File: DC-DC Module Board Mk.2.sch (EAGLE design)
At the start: 151 parts, among them T1 FDN340P, T2 AP1117_LIN_REG, U3 LM1085IS-5.0

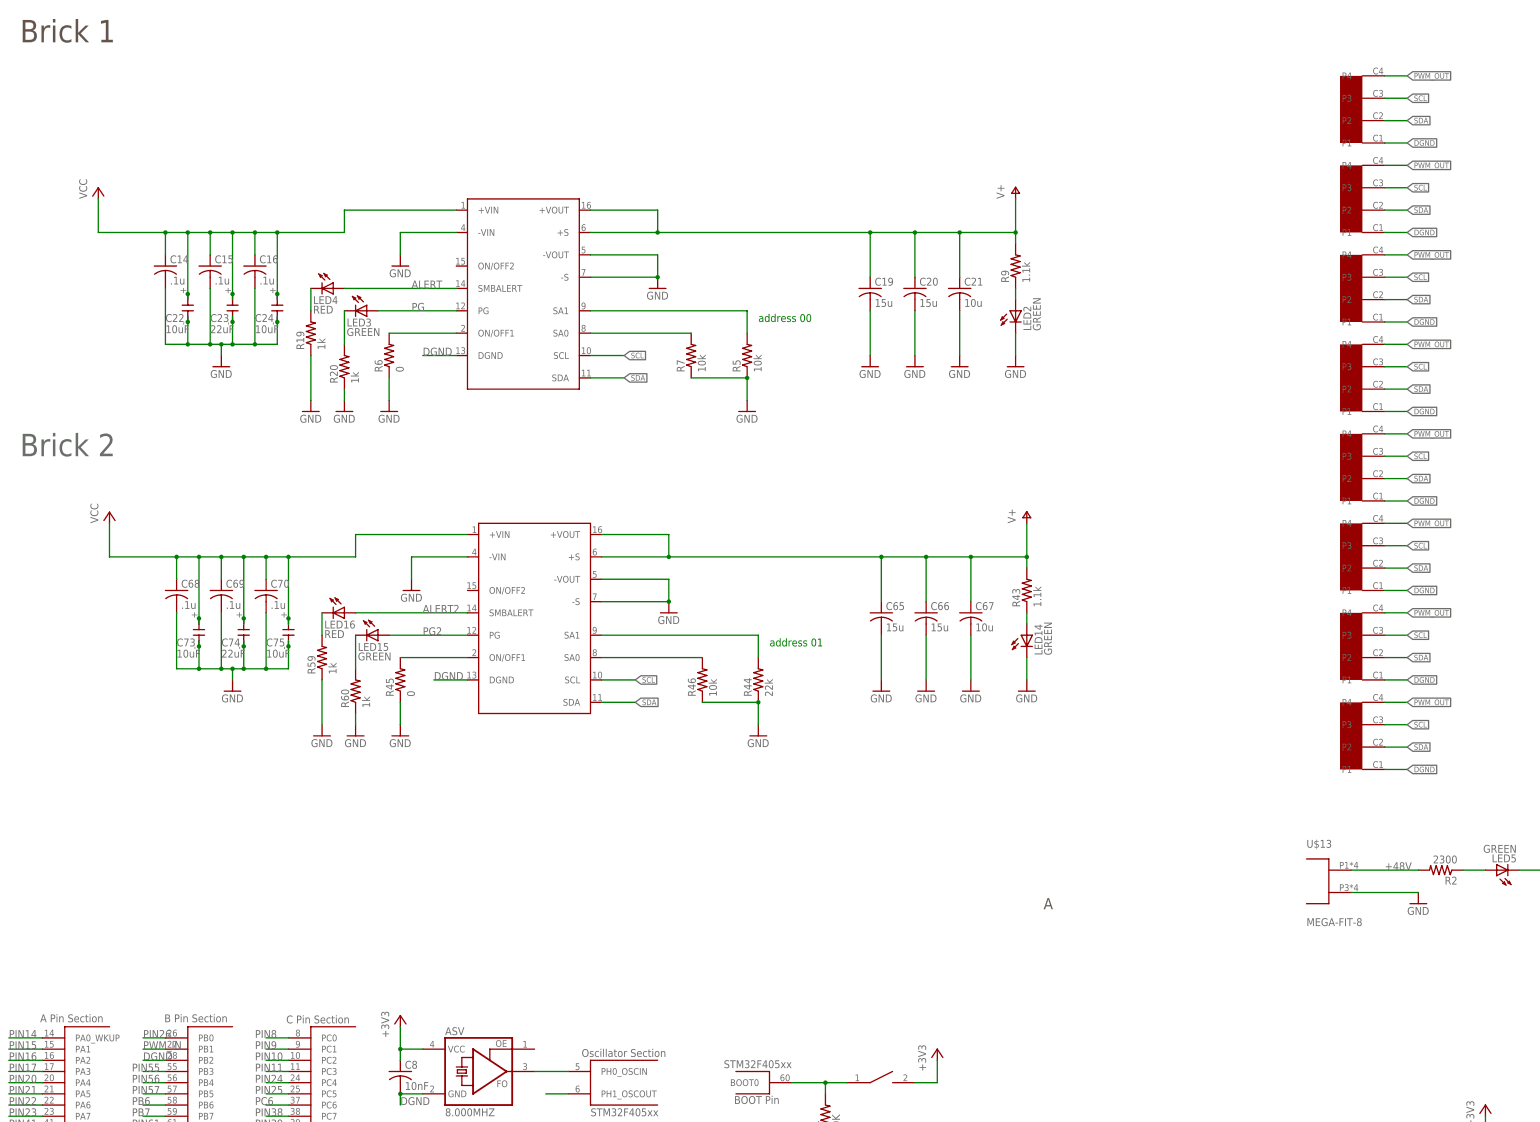
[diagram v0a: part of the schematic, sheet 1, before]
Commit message: changed pwm signal to thrusters
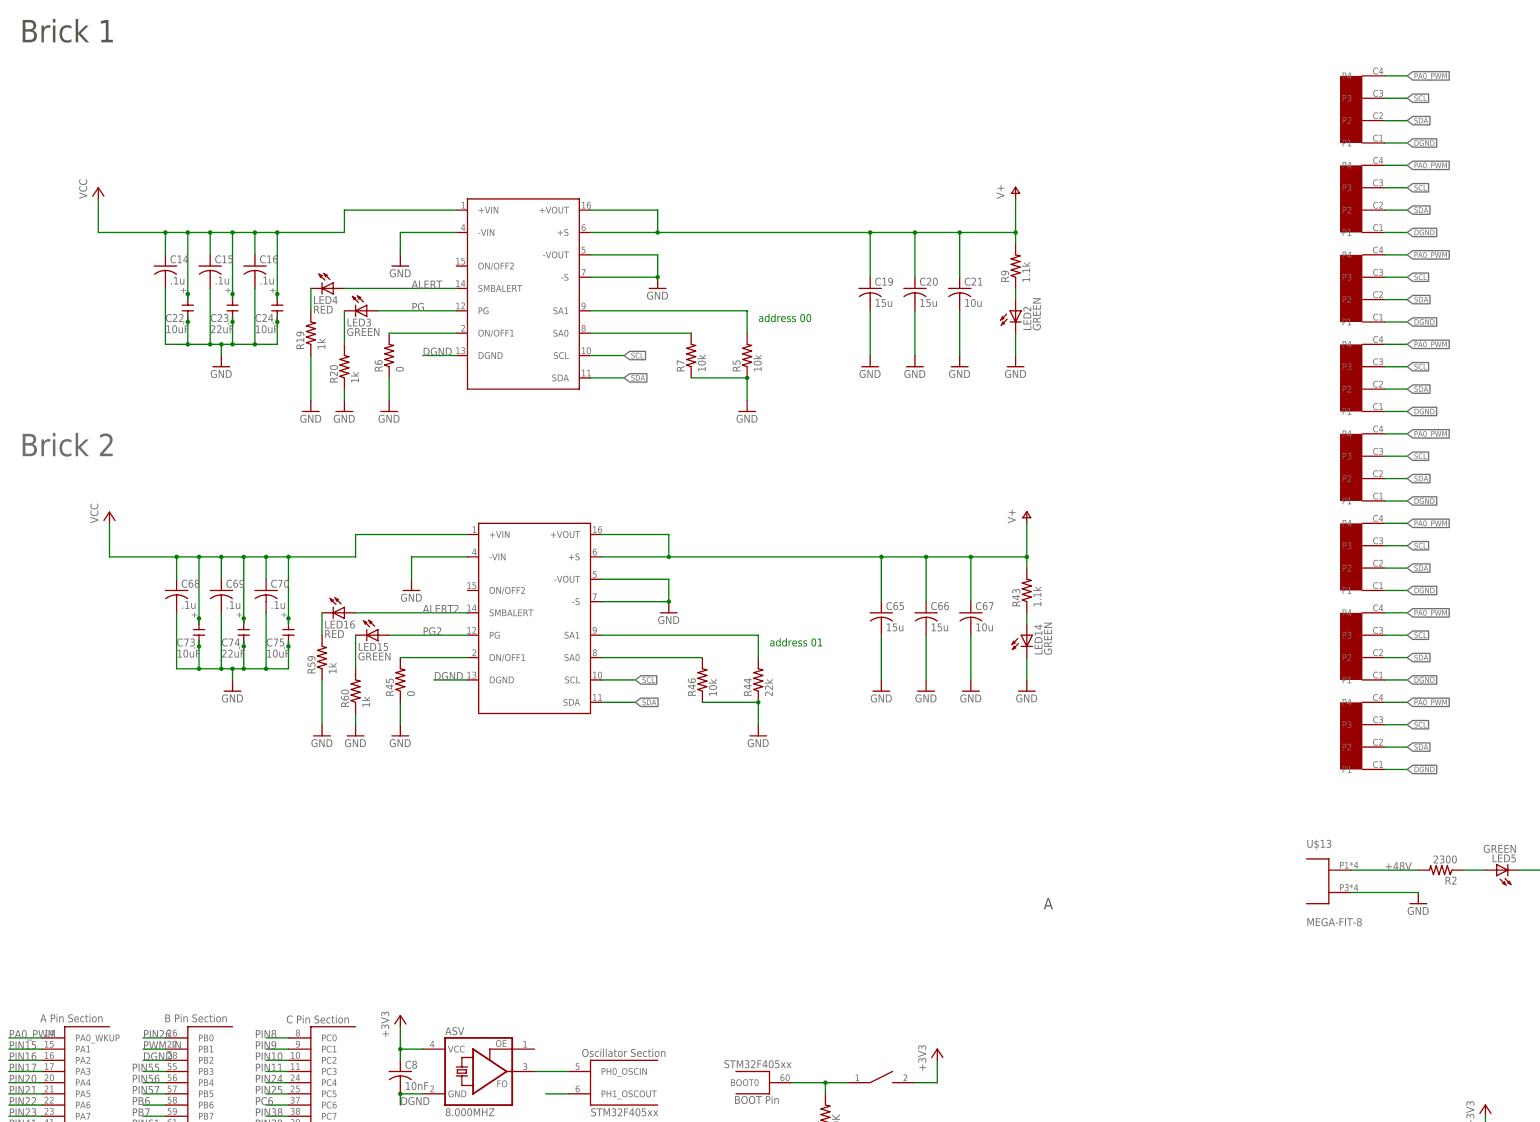
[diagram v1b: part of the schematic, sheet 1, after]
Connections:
- removed net PIN14: U$5G$1.PA0_WKUP
- new net PA0_PWM: U$15.P4, U$20.P4, U$23.P4, U$24.P4, U$25.P4, U$26.P4, U$27.P4, U$28.P4, U$5G$1.PA0_WKUP
- net PWM_OUT: no longer U$15.P4, U$20.P4, U$23.P4, U$24.P4, U$25.P4, U$26.P4, U$27.P4, U$28.P4
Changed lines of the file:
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@@
 </segment>
 </net>
-<net name="PIN14" class="0">
+<net name="PA0_PWM" class="0">
 <segment>
 <pinref part="U$5" gate="G$1" pin="PA0_WKUP"/>
 <wire x1="17.78" y1="-17.78" x2="10.16" y2="-17.78" width="0.1524" layer="91"/>
 <label x="10.16" y="-17.78" size="1.778" layer="95"/>
+</segment>
+<segment>
+<pinref part="U$20" gate="G$1" pin="P4"/>
+<wire x1="322.58" y1="180.34" x2="327.66" y2="180.34" width="0.1524" layer="91"/>
+<label x="327.66" y="180.34" size="1.27" layer="95" xref="yes"/>
+</segment>
+<segment>
+<pinref part="U$15" gate="G$1" pin="P4"/>
+<wire x1="322.58" y1="200.66" x2="327.66" y2="200.66" width="0.1524" layer="91"/>
+<label x="327.66" y="200.66" size="1.27" layer="95" xref="yes"/>
+</segment>
+<segment>
+<pinref part="U$23" gate="G$1" pin="P4"/>
+<wire x1="322.58" y1="160.02" x2="327.66" y2="160.02" width="0.1524" layer="91"/>
+<label x="327.66" y="160.02" size="1.27" layer="95" xref="yes"/>
+</segment>
+<segment>
+<pinref part="U$24" gate="G$1" pin="P4"/>
+<wire x1="322.58" y1="139.7" x2="327.66" y2="139.7" width="0.1524" layer="91"/>
+<label x="327.66" y="139.7" size="1.27" layer="95" xref="yes"/>
+</segment>
+<segment>
+<pinref part="U$25" gate="G$1" pin="P4"/>
+<wire x1="322.58" y1="119.38" x2="327.66" y2="119.38" width="0.1524" layer="91"/>
+<label x="327.66" y="119.38" size="1.27" layer="95" xref="yes"/>
+</segment>
+<segment>
+<pinref part="U$26" gate="G$1" pin="P4"/>
+<wire x1="322.58" y1="99.06" x2="327.66" y2="99.06" width="0.1524" layer="91"/>
+<label x="327.66" y="99.06" size="1.27" layer="95" xref="yes"/>
+</segment>
+<segment>
+<pinref part="U$27" gate="G$1" pin="P4"/>
+<wire x1="322.58" y1="78.74" x2="327.66" y2="78.74" width="0.1524" layer="91"/>
+<label x="327.66" y="78.74" size="1.27" layer="95" xref="yes"/>
+</segment>
+<segment>
+<pinref part="U$28" gate="G$1" pin="P4"/>
+<wire x1="322.58" y1="58.42" x2="327.66" y2="58.42" width="0.1524" layer="91"/>
+<label x="327.66" y="58.42" size="1.27" layer="95" xref="yes"/>
 </segment>
 </net>
@@
 <label x="441.96" y="167.64" size="1.27" layer="95" xref="yes"/>
 </segment>
-<segment>
-<pinref part="U$28" gate="G$1" pin="P4"/>
-<wire x1="322.58" y1="58.42" x2="327.66" y2="58.42" width="0.1524" layer="91"/>
-<label x="327.66" y="58.42" size="1.27" layer="95" xref="yes"/>
-</segment>
-<segment>
-<pinref part="U$15" gate="G$1" pin="P4"/>
-<wire x1="322.58" y1="200.66" x2="327.66" y2="200.66" width="0.1524" layer="91"/>
-<label x="327.66" y="200.66" size="1.27" layer="95" xref="yes"/>
-</segment>
-<segment>
-<pinref part="U$20" gate="G$1" pin="P4"/>
-<wire x1="322.58" y1="180.34" x2="327.66" y2="180.34" width="0.1524" layer="91"/>
-<label x="327.66" y="180.34" size="1.27" layer="95" xref="yes"/>
-</segment>
-<segment>
-<pinref part="U$23" gate="G$1" pin="P4"/>
-<wire x1="322.58" y1="160.02" x2="327.66" y2="160.02" width="0.1524" layer="91"/>
-<label x="327.66" y="160.02" size="1.27" layer="95" xref="yes"/>
-</segment>
-<segment>
-<pinref part="U$24" gate="G$1" pin="P4"/>
-<wire x1="322.58" y1="139.7" x2="327.66" y2="139.7" width="0.1524" layer="91"/>
-<label x="327.66" y="139.7" size="1.27" layer="95" xref="yes"/>
-</segment>
-<segment>
-<pinref part="U$25" gate="G$1" pin="P4"/>
-<wire x1="322.58" y1="119.38" x2="327.66" y2="119.38" width="0.1524" layer="91"/>
-<label x="327.66" y="119.38" size="1.27" layer="95" xref="yes"/>
-</segment>
-<segment>
-<pinref part="U$26" gate="G$1" pin="P4"/>
-<wire x1="322.58" y1="99.06" x2="327.66" y2="99.06" width="0.1524" layer="91"/>
-<label x="327.66" y="99.06" size="1.27" layer="95" xref="yes"/>
-</segment>
-<segment>
-<pinref part="U$27" gate="G$1" pin="P4"/>
-<wire x1="322.58" y1="78.74" x2="327.66" y2="78.74" width="0.1524" layer="91"/>
-<label x="327.66" y="78.74" size="1.27" layer="95" xref="yes"/>
-</segment>
-</net>
+</net>

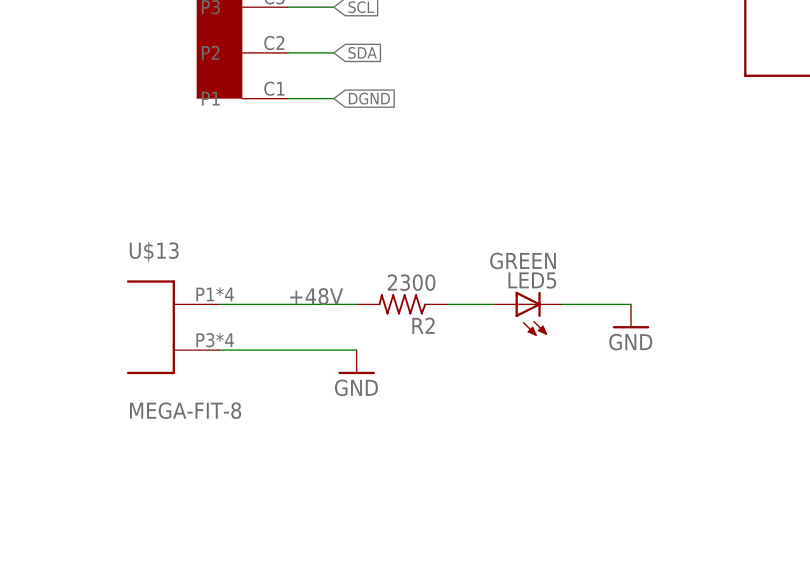
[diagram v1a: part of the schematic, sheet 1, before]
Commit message: sizing and aesthetic changes
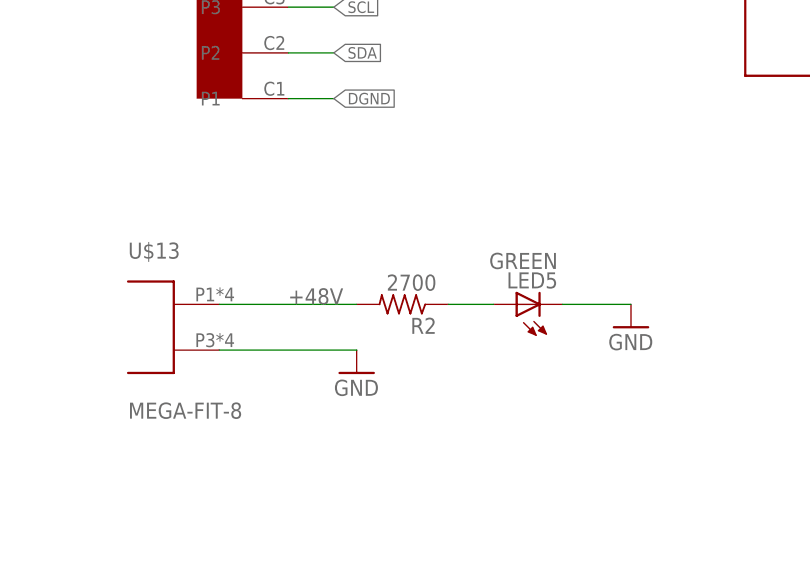
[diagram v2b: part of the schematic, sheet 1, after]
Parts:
- R2: value 2300 -> 2700
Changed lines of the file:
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@@
 <attribute name="PARTNO" value="160-1446-1-ND"/>
 </part>
-<part name="R2" library="resistor" deviceset="R-US_" device="R2512" value="2300">
+<part name="R2" library="resistor" deviceset="R-US_" device="R2512" value="2700">
 <attribute name="BOM" value="INCLUDE"/>
 <attribute name="PARTNO" value="RHC2512FT2K20CT-ND"/>

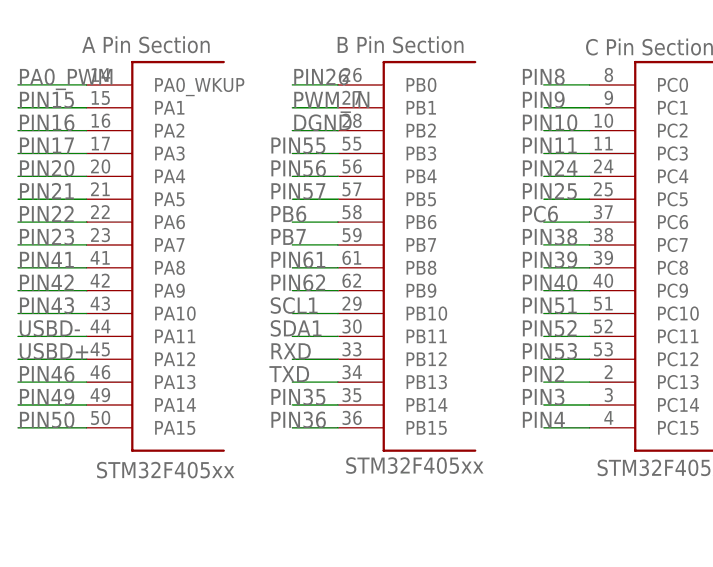
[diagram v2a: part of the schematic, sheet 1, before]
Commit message: Changed pins for i2c
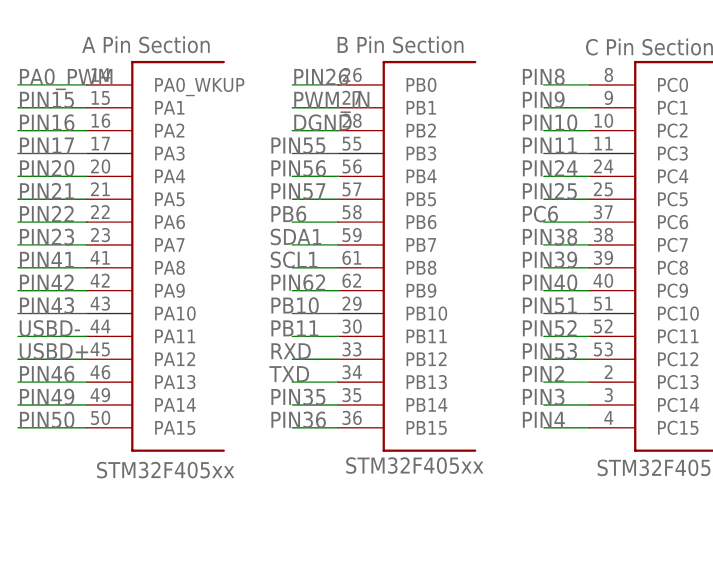
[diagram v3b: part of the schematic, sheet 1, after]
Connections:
- removed net PB7: U$5G$2.PB7
- removed net PIN61: U$5G$2.PB8
- new net PB10: U$5G$2.PB10
- new net PB11: U$5G$2.PB11
- net SCL1: now also U$5G$2.PB8; no longer U$5G$2.PB10
- net SDA1: now also U$5G$2.PB7; no longer U$5G$2.PB11
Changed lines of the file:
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@@
 <?xml version="1.0" encoding="utf-8"?>
 <!DOCTYPE eagle SYSTEM "eagle.dtd">
-<eagle version="7.4.0">
+<eagle version="7.5.0">
 <drawing>
 <settings>
@@
 </segment>
 </net>
-<net name="PIN61" class="0">
-<segment>
-<pinref part="U$5" gate="G$2" pin="PB8"/>
-<wire x1="45.72" y1="-38.1" x2="40.64" y2="-38.1" width="0.1524" layer="91"/>
-<label x="38.1" y="-38.1" size="1.778" layer="95"/>
-</segment>
-</net>
 <net name="PIN62" class="0">
 <segment>
@@
 </segment>
 <segment>
-<pinref part="U$5" gate="G$2" pin="PB11"/>
-<wire x1="45.72" y1="-45.72" x2="40.64" y2="-45.72" width="0.1524" layer="91"/>
-<label x="38.1" y="-45.72" size="1.778" layer="95"/>
+<pinref part="U$5" gate="G$2" pin="PB7"/>
+<wire x1="45.72" y1="-35.56" x2="40.64" y2="-35.56" width="0.1524" layer="91"/>
+<label x="38.1" y="-35.56" size="1.778" layer="95"/>
 </segment>
 </net>
@@
 </segment>
 <segment>
-<pinref part="U$5" gate="G$2" pin="PB10"/>
-<wire x1="45.72" y1="-43.18" x2="40.64" y2="-43.18" width="0.1524" layer="91"/>
-<label x="38.1" y="-43.18" size="1.778" layer="95"/>
+<pinref part="U$5" gate="G$2" pin="PB8"/>
+<wire x1="45.72" y1="-38.1" x2="40.64" y2="-38.1" width="0.1524" layer="91"/>
+<label x="38.1" y="-38.1" size="1.778" layer="95"/>
 </segment>
 </net>
@@
 </segment>
 </net>
-<net name="PB7" class="0">
-<segment>
-<pinref part="U$5" gate="G$2" pin="PB7"/>
-<wire x1="45.72" y1="-35.56" x2="40.64" y2="-35.56" width="0.1524" layer="91"/>
-<label x="38.1" y="-35.56" size="1.778" layer="95"/>
-</segment>
-</net>
+<net name="PB10" class="0">
+<segment>
+<pinref part="U$5" gate="G$2" pin="PB10"/>
+<wire x1="45.72" y1="-43.18" x2="40.64" y2="-43.18" width="0.1524" layer="91"/>
+<label x="38.1" y="-43.18" size="1.778" layer="95"/>
+</segment>
+</net>
+<net name="PB11" class="0">
+<segment>
+<pinref part="U$5" gate="G$2" pin="PB11"/>
+<wire x1="45.72" y1="-45.72" x2="40.64" y2="-45.72" width="0.1524" layer="91"/>
+<label x="38.1" y="-45.72" size="1.778" layer="95"/>
+</segment>
+</net>
